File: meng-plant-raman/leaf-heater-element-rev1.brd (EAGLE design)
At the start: 20.3 x 10.2 mm, 4 parts, among them IC1 MAX30205MTA+, X1 SM06B-SRSS-TB

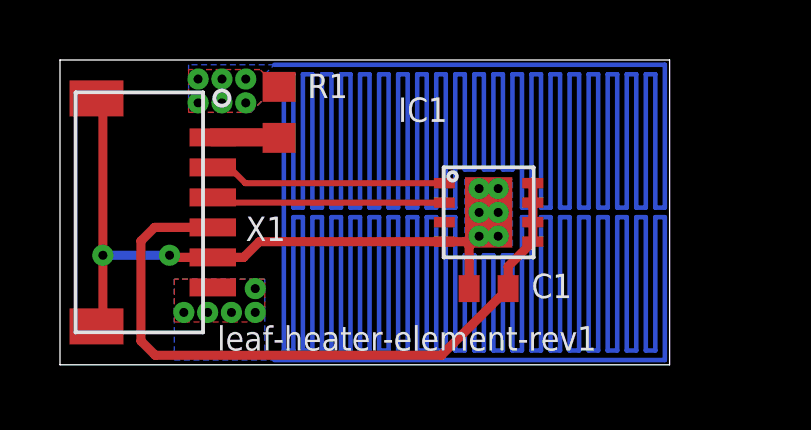
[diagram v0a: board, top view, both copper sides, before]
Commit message: Modified leaf-heater and triax-passthrough for second sendout
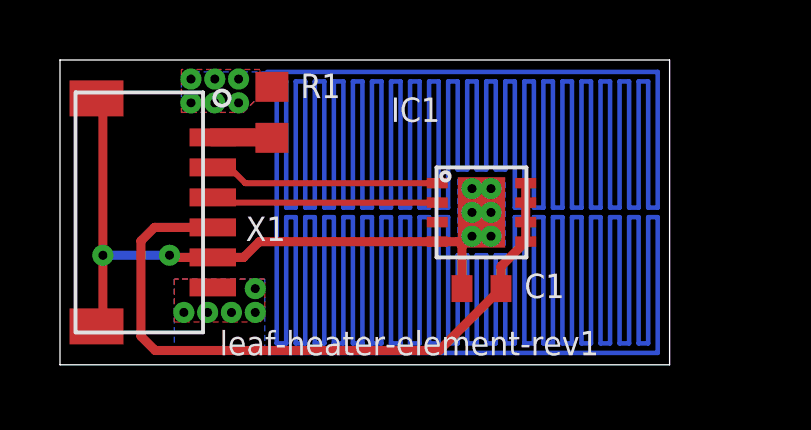
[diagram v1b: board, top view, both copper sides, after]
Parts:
- moved C1 0.24 mm to (14.0, 2.54)
- moved IC1 0.24 mm to (14.0, 5.08)
- moved R1 0.24 mm to (7.06, 8.41)
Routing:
- net GND: track 401.6 -> 382.1 mm
